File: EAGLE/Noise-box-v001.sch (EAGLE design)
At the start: 2 parts, among them J1 AVR_SPI_PROG_3X22X3_LOCK, U1 ATMEGA328P_TQFP

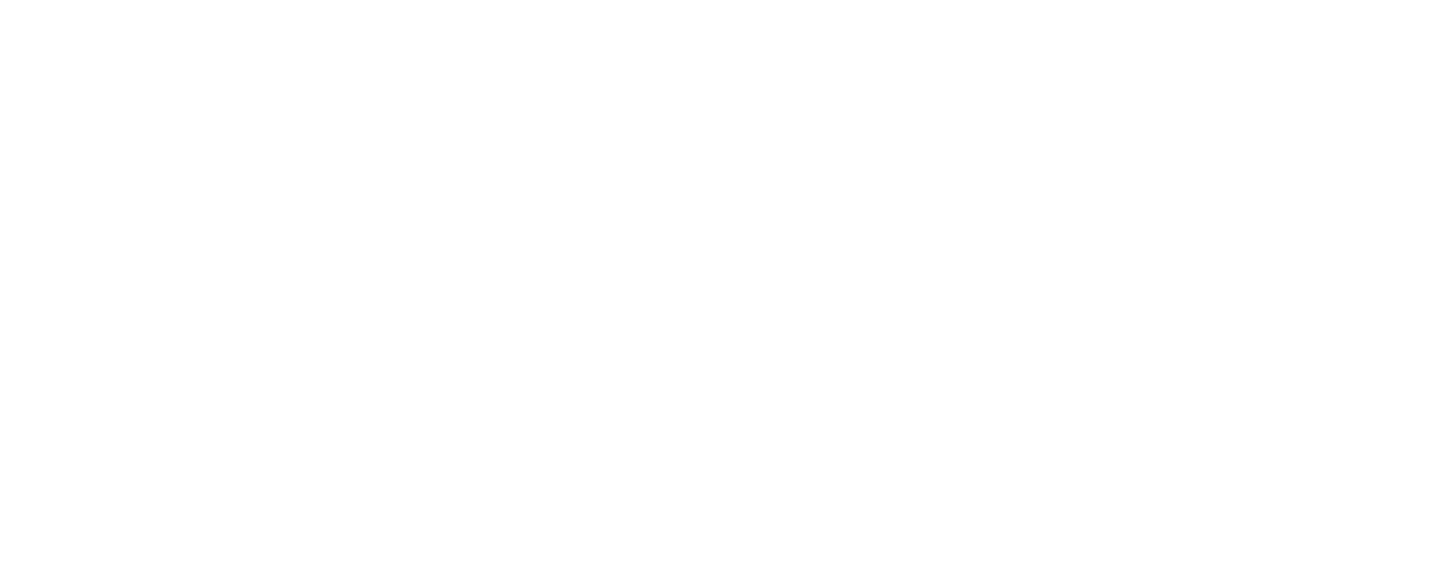
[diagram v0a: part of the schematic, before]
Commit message: Sch update - power
Added voltage regulators and supporting components.
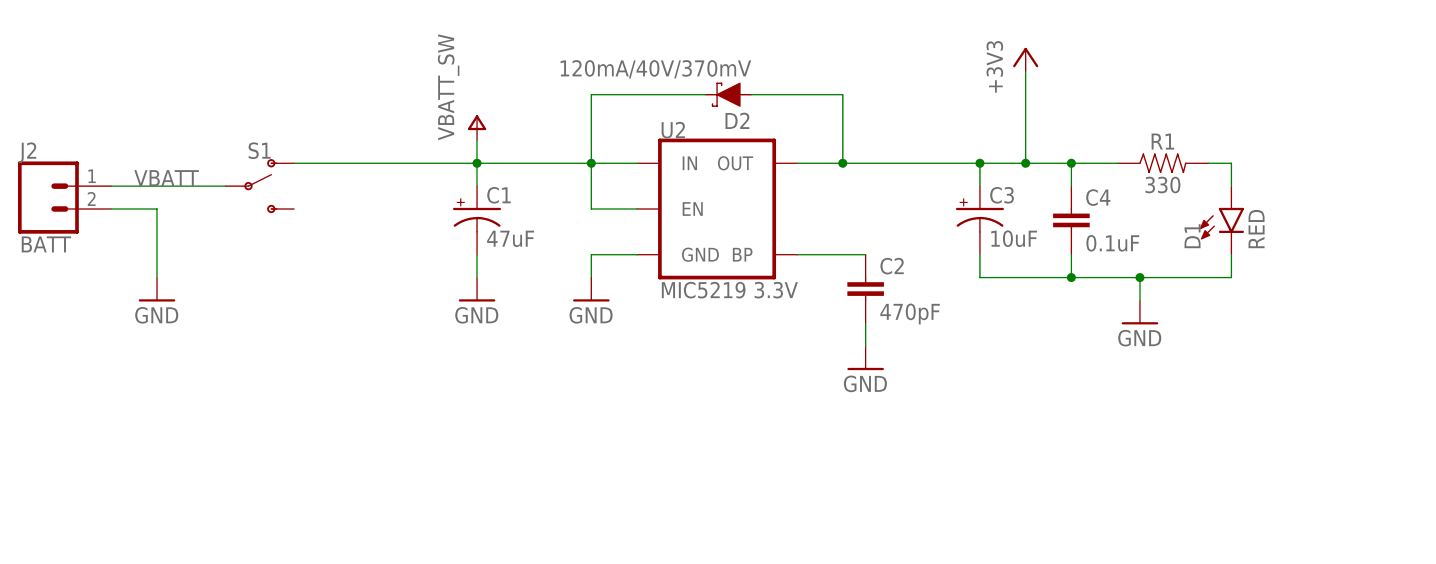
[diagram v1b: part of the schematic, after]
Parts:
- added C1: 47uF, SparkFun-Capacitors:47UF-POLAR-EIA3528-10V-10%
- added C2: 470pF, SparkFun-Capacitors:470PF-0603-50V-5%
- added C3: 10uF, SparkFun-Capacitors:10UF-POLAR-EIA3216-16V-10%(TANT)
- added C4: 0.1uF, SparkFun-Capacitors:0.1UF-0603-25V-5%
- added D1: RED, SparkFun-LED:LED-RED0603
- added D2: 120mA/40V/370mV, SparkFun-DiscreteSemi:DIODE-SCHOTTKY-RB751S40
- added J2: BATT, SparkFun-Connectors:CONN_02-JST-2MM-SMT
- added R1: 330, SparkFun-Resistors:330OHM-0603-1/10W-1%
- added S1: (no value), SparkFun-Switches:SWITCH-SPDT-SMD-RIGHT-ANGLE
- added U2: MIC5219 3.3V, SparkFun-IC-Power:V_REG_MIC52193.3V
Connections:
- new net N$2: C2.1, U2.BP
- new net N$3: D1.A, R1.2
- new net V+: C1.+, D2.C, S1.O, U2.EN, U2.IN
- new net VBATT: J2.2, S1.P
- net +3V3: now also C3.+, C4.1, D2.A, R1.1, U2.OUT
- net GND: now also C1.-, C2.2, C3.-, C4.2, D1.C, J2.1, U2.GND
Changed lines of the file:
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@@
 <part name="GND1" library="supply1" deviceset="GND" device=""/>
 <part name="J1" library="SparkFun-Connectors" deviceset="AVR_SPI_PROG_3X2" device="2X3_LOCK"/>
+<part name="J2" library="SparkFun-Connectors" deviceset="CONN_02" device="-JST-2MM-SMT" value="BATT"/>
+<part name="S1" library="SparkFun-Switches" deviceset="SWITCH-SPDT" device="-SMD-RIGHT-ANGLE"/>
+<part name="GND2" library="supply1" deviceset="GND" device=""/>
+<part name="GND3" library="supply1" deviceset="GND" device=""/>
+<part name="P+1" library="supply1" deviceset="V+" device="" value="VBATT_SW"/>
+<part name="C1" library="SparkFun-Capacitors" deviceset="47UF-POLAR" device="-EIA3528-10V-10%" value="47uF"/>
+<part name="U2" library="SparkFun-IC-Power" deviceset="V_REG_MIC5219" device="3.3V" value="MIC5219 3.3V"/>
+<part name="GND4" library="supply1" deviceset="GND" device=""/>
+<part name="C2" library="SparkFun-Capacitors" deviceset="470PF" device="-0603-50V-5%" value="470pF"/>
+<part name="GND5" library="supply1" deviceset="GND" device=""/>
+<part name="C3" library="SparkFun-Capacitors" deviceset="10UF-POLAR" device="-EIA3216-16V-10%(TANT)" value="10uF"/>
+<part name="C4" library="SparkFun-Capacitors" deviceset="0.1UF" device="-0603-25V-5%" value="0.1uF"/>
+<part name="R1" library="SparkFun-Resistors" deviceset="330OHM" device="-0603-1/10W-1%" value="330"/>
+<part name="D1" library="SparkFun-LED" deviceset="LED-RED" device="0603" value="RED"/>
+<part name="GND6" library="supply1" deviceset="GND" device=""/>
+<part name="D2" library="SparkFun-DiscreteSemi" deviceset="DIODE-SCHOTTKY" device="-RB751S40" value="120mA/40V/370mV"/>
+<part name="+3V2" library="supply1" deviceset="+3V3" device=""/>
 </parts>
 <sheets>
@@
 <instance part="GND1" gate="1" x="198.12" y="132.08"/>
 <instance part="J1" gate="G$1" x="66.04" y="170.18"/>
+<instance part="J2" gate="G$1" x="22.86" y="251.46"/>
+<instance part="S1" gate="1" x="45.72" y="254"/>
+<instance part="GND2" gate="1" x="35.56" y="241.3"/>
+<instance part="GND3" gate="1" x="71.12" y="241.3"/>
+<instance part="P+1" gate="1" x="71.12" y="261.62"/>
+<instance part="C1" gate="G$1" x="71.12" y="251.46"/>
+<instance part="U2" gate="G$1" x="99.06" y="251.46"/>
+<instance part="GND4" gate="1" x="83.82" y="241.3"/>
+<instance part="C2" gate="G$1" x="114.3" y="241.3"/>
+<instance part="GND5" gate="1" x="114.3" y="233.68"/>
+<instance part="C3" gate="G$1" x="127" y="251.46"/>
+<instance part="C4" gate="G$1" x="137.16" y="248.92"/>
+<instance part="R1" gate="G$1" x="147.32" y="256.54"/>
+<instance part="D1" gate="G$1" x="154.94" y="251.46"/>
+<instance part="GND6" gate="1" x="144.78" y="238.76"/>
+<instance part="D2" gate="G$1" x="99.06" y="264.16" rot="R180"/>
+<instance part="+3V2" gate="G$1" x="132.08" y="269.24"/>
 </instances>
 <busses>
@@
 <label x="88.9" y="172.72" size="1.778" layer="95" rot="MR0"/>
 </segment>
+<segment>
+<pinref part="U2" gate="G$1" pin="OUT"/>
+<pinref part="R1" gate="G$1" pin="1"/>
+<wire x1="106.68" y1="256.54" x2="111.76" y2="256.54" width="0.1524" layer="91"/>
+<pinref part="C3" gate="G$1" pin="+"/>
+<wire x1="111.76" y1="256.54" x2="127" y2="256.54" width="0.1524" layer="91"/>
+<wire x1="127" y1="256.54" x2="132.08" y2="256.54" width="0.1524" layer="91"/>
+<wire x1="132.08" y1="256.54" x2="137.16" y2="256.54" width="0.1524" layer="91"/>
+<wire x1="137.16" y1="256.54" x2="142.24" y2="256.54" width="0.1524" layer="91"/>
+<wire x1="127" y1="254" x2="127" y2="256.54" width="0.1524" layer="91"/>
+<junction x="127" y="256.54"/>
+<pinref part="C4" gate="G$1" pin="1"/>
+<wire x1="137.16" y1="254" x2="137.16" y2="256.54" width="0.1524" layer="91"/>
+<junction x="137.16" y="256.54"/>
+<pinref part="D2" gate="G$1" pin="A"/>
+<wire x1="111.76" y1="256.54" x2="111.76" y2="264.16" width="0.1524" layer="91"/>
+<wire x1="111.76" y1="264.16" x2="101.6" y2="264.16" width="0.1524" layer="91"/>
+<junction x="111.76" y="256.54"/>
+<pinref part="+3V2" gate="G$1" pin="+3V3"/>
+<wire x1="132.08" y1="256.54" x2="132.08" y2="266.7" width="0.1524" layer="91"/>
+<junction x="132.08" y="256.54"/>
+</segment>
 </net>
 <net name="GND" class="0">
@@
 <label x="88.9" y="167.64" size="1.778" layer="95" rot="MR0"/>
 </segment>
+<segment>
+<pinref part="J2" gate="G$1" pin="1"/>
+<pinref part="GND2" gate="1" pin="GND"/>
+<wire x1="30.48" y1="251.46" x2="35.56" y2="251.46" width="0.1524" layer="91"/>
+<wire x1="35.56" y1="251.46" x2="35.56" y2="243.84" width="0.1524" layer="91"/>
+</segment>
+<segment>
+<pinref part="GND3" gate="1" pin="GND"/>
+<pinref part="C1" gate="G$1" pin="-"/>
+<wire x1="71.12" y1="243.84" x2="71.12" y2="246.38" width="0.1524" layer="91"/>
+</segment>
+<segment>
+<pinref part="U2" gate="G$1" pin="GND"/>
+<wire x1="88.9" y1="246.38" x2="83.82" y2="246.38" width="0.1524" layer="91"/>
+<wire x1="83.82" y1="246.38" x2="83.82" y2="243.84" width="0.1524" layer="91"/>
+<pinref part="GND4" gate="1" pin="GND"/>
+</segment>
+<segment>
+<pinref part="C2" gate="G$1" pin="2"/>
+<wire x1="114.3" y1="238.76" x2="114.3" y2="236.22" width="0.1524" layer="91"/>
+<pinref part="GND5" gate="1" pin="GND"/>
+</segment>
+<segment>
+<pinref part="C4" gate="G$1" pin="2"/>
+<wire x1="137.16" y1="246.38" x2="137.16" y2="243.84" width="0.1524" layer="91"/>
+<pinref part="C3" gate="G$1" pin="-"/>
+<wire x1="127" y1="246.38" x2="127" y2="243.84" width="0.1524" layer="91"/>
+<wire x1="127" y1="243.84" x2="137.16" y2="243.84" width="0.1524" layer="91"/>
+<pinref part="D1" gate="G$1" pin="C"/>
+<wire x1="154.94" y1="246.38" x2="154.94" y2="243.84" width="0.1524" layer="91"/>
+<wire x1="137.16" y1="243.84" x2="144.78" y2="243.84" width="0.1524" layer="91"/>
+<junction x="137.16" y="243.84"/>
+<pinref part="GND6" gate="1" pin="GND"/>
+<wire x1="144.78" y1="243.84" x2="154.94" y2="243.84" width="0.1524" layer="91"/>
+<wire x1="144.78" y1="241.3" x2="144.78" y2="243.84" width="0.1524" layer="91"/>
+<junction x="144.78" y="243.84"/>
+</segment>
 </net>
 <net name="MOSI" class="0">
@@
 </segment>
 </net>
+<net name="VBATT" class="0">
+<segment>
+<pinref part="J2" gate="G$1" pin="2"/>
+<pinref part="S1" gate="1" pin="P"/>
+<wire x1="30.48" y1="254" x2="43.18" y2="254" width="0.1524" layer="91"/>
+<label x="33.02" y="254" size="1.778" layer="95"/>
+</segment>
+</net>
+<net name="V+" class="0">
+<segment>
+<pinref part="P+1" gate="1" pin="V+"/>
+<pinref part="C1" gate="G$1" pin="+"/>
+<wire x1="71.12" y1="259.08" x2="71.12" y2="256.54" width="0.1524" layer="91"/>
+<pinref part="S1" gate="1" pin="O"/>
+<wire x1="71.12" y1="256.54" x2="71.12" y2="254" width="0.1524" layer="91"/>
+<wire x1="50.8" y1="256.54" x2="71.12" y2="256.54" width="0.1524" layer="91"/>
+<junction x="71.12" y="256.54"/>
+<pinref part="U2" gate="G$1" pin="IN"/>
+<wire x1="71.12" y1="256.54" x2="83.82" y2="256.54" width="0.1524" layer="91"/>
+<pinref part="U2" gate="G$1" pin="EN"/>
+<wire x1="83.82" y1="256.54" x2="88.9" y2="256.54" width="0.1524" layer="91"/>
+<wire x1="88.9" y1="251.46" x2="83.82" y2="251.46" width="0.1524" layer="91"/>
+<wire x1="83.82" y1="251.46" x2="83.82" y2="256.54" width="0.1524" layer="91"/>
+<junction x="83.82" y="256.54"/>
+<pinref part="D2" gate="G$1" pin="C"/>
+<wire x1="96.52" y1="264.16" x2="83.82" y2="264.16" width="0.1524" layer="91"/>
+<wire x1="83.82" y1="264.16" x2="83.82" y2="256.54" width="0.1524" layer="91"/>
+</segment>
+</net>
+<net name="N$2" class="0">
+<segment>
+<pinref part="U2" gate="G$1" pin="BP"/>
+<pinref part="C2" gate="G$1" pin="1"/>
+<wire x1="106.68" y1="246.38" x2="114.3" y2="246.38" width="0.1524" layer="91"/>
+</segment>
+</net>
+<net name="N$3" class="0">
+<segment>
+<pinref part="R1" gate="G$1" pin="2"/>
+<pinref part="D1" gate="G$1" pin="A"/>
+<wire x1="152.4" y1="256.54" x2="154.94" y2="256.54" width="0.1524" layer="91"/>
+<wire x1="154.94" y1="256.54" x2="154.94" y2="254" width="0.1524" layer="91"/>
+</segment>
+</net>

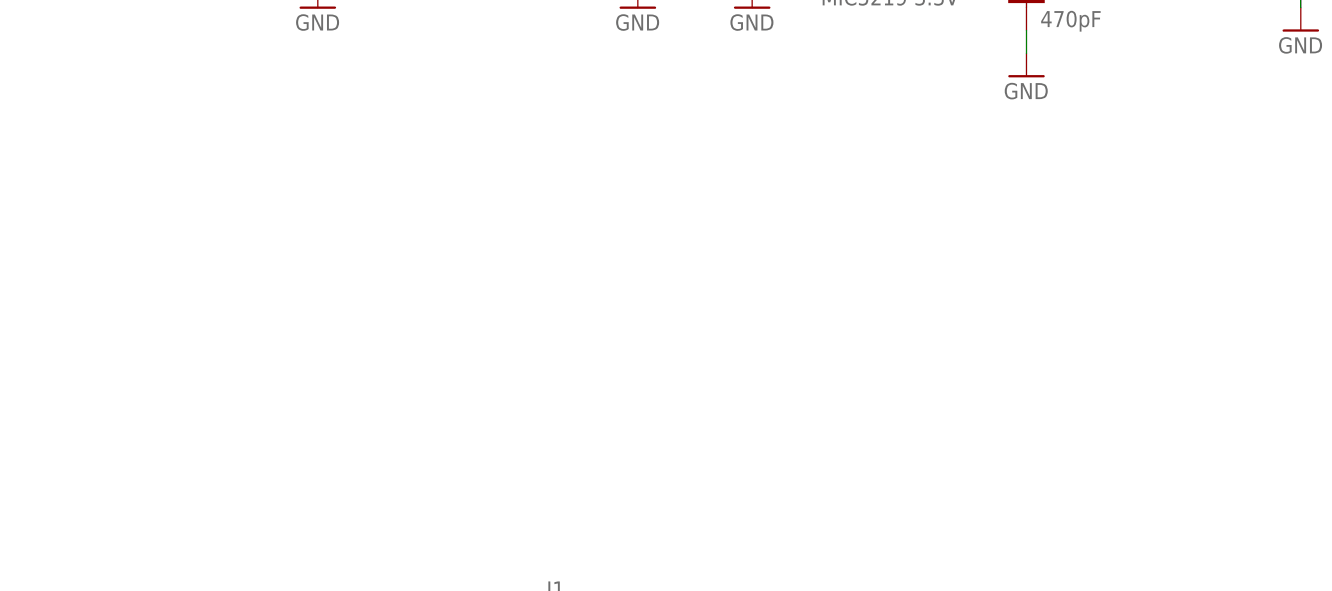
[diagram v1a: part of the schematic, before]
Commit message: Schematic work
Added regulator, battery charging circuit
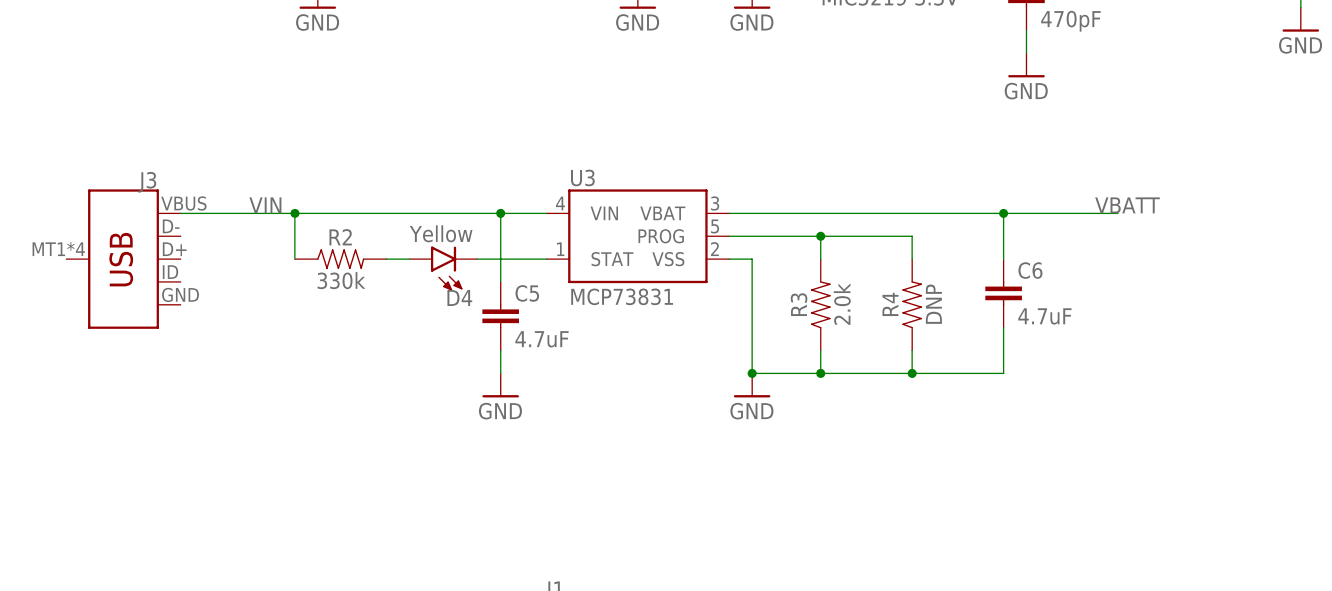
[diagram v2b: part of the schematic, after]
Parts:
- added C5, C6: 4.7uF, SparkFun-Capacitors:4.7UF0603
- added D4: Yellow, SparkFun-LED:LED-YELLOW0603
- added J3: (no value), SparkFun-Connectors:USB_MICRO-B_SMT
- added R2: 330k, SparkFun-Resistors:330KOHM-0603-1/10W-1%
- added R3: 2.0k, SparkFun-Resistors:2.0KOHM-0603-1/10W-5%
- added R4: DNP, SparkFun-Resistors:2.0KOHM-0603-1/10W-5%
- added U3: MCP73831, SparkFun-IC-Power:MCP73831
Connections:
- new net N$1: D4.A, R2.2
- new net N$4: R3.2, R4.2, U3.PROG
- new net N$5: D4.C, U3.STAT
- new net VIN: C5.1, J3.VBUS, R2.1, U3.VIN
- net GND: now also C5.2, C6.2, R3.1, R4.1, U3.VSS
- net VBATT: now also C6.1, U3.VBAT
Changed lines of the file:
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@@
 <part name="D2" library="SparkFun-DiscreteSemi" deviceset="DIODE-SCHOTTKY" device="-RB751S40" value="120mA/40V/370mV"/>
 <part name="+3V2" library="supply1" deviceset="+3V3" device=""/>
+<part name="J3" library="SparkFun-Connectors" deviceset="USB_MICRO-B" device="_SMT"/>
+<part name="U3" library="SparkFun-IC-Power" deviceset="MCP73831" device=""/>
+<part name="D4" library="SparkFun-LED" deviceset="LED-YELLOW" device="0603" value="Yellow"/>
+<part name="R2" library="SparkFun-Resistors" deviceset="330KOHM" device="-0603-1/10W-1%" value="330k"/>
+<part name="C5" library="SparkFun-Capacitors" deviceset="4.7UF" device="0603" value="4.7uF"/>
+<part name="R3" library="SparkFun-Resistors" deviceset="2.0KOHM" device="-0603-1/10W-5%" value="2.0k"/>
+<part name="R4" library="SparkFun-Resistors" deviceset="2.0KOHM" device="-0603-1/10W-5%" value="DNP"/>
+<part name="C6" library="SparkFun-Capacitors" deviceset="4.7UF" device="0603" value="4.7uF"/>
+<part name="GND7" library="supply1" deviceset="GND" device=""/>
+<part name="GND8" library="supply1" deviceset="GND" device=""/>
 </parts>
 <sheets>
@@
 <instance part="D2" gate="G$1" x="99.06" y="264.16" rot="R180"/>
 <instance part="+3V2" gate="G$1" x="132.08" y="269.24"/>
+<instance part="J3" gate="G$1" x="15.24" y="213.36" rot="MR0"/>
+<instance part="U3" gate="G$1" x="71.12" y="215.9"/>
+<instance part="D4" gate="G$1" x="48.26" y="213.36" rot="R90"/>
+<instance part="R2" gate="G$1" x="38.1" y="213.36"/>
+<instance part="C5" gate="G$1" x="55.88" y="205.74"/>
+<instance part="R3" gate="G$1" x="91.44" y="208.28" rot="R90"/>
+<instance part="R4" gate="G$1" x="101.6" y="208.28" rot="R90"/>
+<instance part="C6" gate="G$1" x="111.76" y="208.28"/>
+<instance part="GND7" gate="1" x="55.88" y="198.12"/>
+<instance part="GND8" gate="1" x="83.82" y="198.12"/>
 </instances>
 <busses>
@@
 <junction x="144.78" y="243.84"/>
 </segment>
+<segment>
+<pinref part="C5" gate="G$1" pin="2"/>
+<pinref part="GND7" gate="1" pin="GND"/>
+<wire x1="55.88" y1="203.2" x2="55.88" y2="200.66" width="0.1524" layer="91"/>
+</segment>
+<segment>
+<pinref part="U3" gate="G$1" pin="VSS"/>
+<pinref part="GND8" gate="1" pin="GND"/>
+<wire x1="81.28" y1="213.36" x2="83.82" y2="213.36" width="0.1524" layer="91"/>
+<wire x1="83.82" y1="213.36" x2="83.82" y2="200.66" width="0.1524" layer="91"/>
+<pinref part="R3" gate="G$1" pin="1"/>
+<wire x1="91.44" y1="203.2" x2="91.44" y2="200.66" width="0.1524" layer="91"/>
+<wire x1="91.44" y1="200.66" x2="83.82" y2="200.66" width="0.1524" layer="91"/>
+<junction x="83.82" y="200.66"/>
+<pinref part="R4" gate="G$1" pin="1"/>
+<wire x1="101.6" y1="203.2" x2="101.6" y2="200.66" width="0.1524" layer="91"/>
+<wire x1="101.6" y1="200.66" x2="91.44" y2="200.66" width="0.1524" layer="91"/>
+<junction x="91.44" y="200.66"/>
+<pinref part="C6" gate="G$1" pin="2"/>
+<wire x1="111.76" y1="205.74" x2="111.76" y2="200.66" width="0.1524" layer="91"/>
+<wire x1="111.76" y1="200.66" x2="101.6" y2="200.66" width="0.1524" layer="91"/>
+<junction x="101.6" y="200.66"/>
+</segment>
 </net>
 <net name="MOSI" class="0">
@@
 <wire x1="30.48" y1="254" x2="43.18" y2="254" width="0.1524" layer="91"/>
 <label x="33.02" y="254" size="1.778" layer="95"/>
+</segment>
+<segment>
+<pinref part="U3" gate="G$1" pin="VBAT"/>
+<wire x1="81.28" y1="218.44" x2="111.76" y2="218.44" width="0.1524" layer="91"/>
+<pinref part="C6" gate="G$1" pin="1"/>
+<wire x1="111.76" y1="218.44" x2="124.46" y2="218.44" width="0.1524" layer="91"/>
+<wire x1="111.76" y1="213.36" x2="111.76" y2="218.44" width="0.1524" layer="91"/>
+<junction x="111.76" y="218.44"/>
+<label x="121.92" y="218.44" size="1.778" layer="95"/>
 </segment>
 </net>
@@
 </segment>
 </net>
+<net name="N$1" class="0">
+<segment>
+<pinref part="R2" gate="G$1" pin="2"/>
+<pinref part="D4" gate="G$1" pin="A"/>
+<wire x1="45.72" y1="213.36" x2="43.18" y2="213.36" width="0.1524" layer="91"/>
+</segment>
+</net>
+<net name="VIN" class="0">
+<segment>
+<pinref part="J3" gate="G$1" pin="VBUS"/>
+<pinref part="C5" gate="G$1" pin="1"/>
+<wire x1="20.32" y1="218.44" x2="33.02" y2="218.44" width="0.1524" layer="91"/>
+<wire x1="33.02" y1="218.44" x2="55.88" y2="218.44" width="0.1524" layer="91"/>
+<wire x1="55.88" y1="218.44" x2="55.88" y2="210.82" width="0.1524" layer="91"/>
+<pinref part="R2" gate="G$1" pin="1"/>
+<wire x1="33.02" y1="213.36" x2="33.02" y2="218.44" width="0.1524" layer="91"/>
+<junction x="33.02" y="218.44"/>
+<pinref part="U3" gate="G$1" pin="VIN"/>
+<wire x1="55.88" y1="218.44" x2="60.96" y2="218.44" width="0.1524" layer="91"/>
+<junction x="55.88" y="218.44"/>
+<label x="27.94" y="218.44" size="1.778" layer="95"/>
+</segment>
+</net>
+<net name="N$5" class="0">
+<segment>
+<pinref part="D4" gate="G$1" pin="C"/>
+<pinref part="U3" gate="G$1" pin="STAT"/>
+<wire x1="53.34" y1="213.36" x2="60.96" y2="213.36" width="0.1524" layer="91"/>
+</segment>
+</net>
+<net name="N$4" class="0">
+<segment>
+<pinref part="U3" gate="G$1" pin="PROG"/>
+<pinref part="R3" gate="G$1" pin="2"/>
+<wire x1="81.28" y1="215.9" x2="91.44" y2="215.9" width="0.1524" layer="91"/>
+<wire x1="91.44" y1="215.9" x2="91.44" y2="213.36" width="0.1524" layer="91"/>
+<pinref part="R4" gate="G$1" pin="2"/>
+<wire x1="91.44" y1="215.9" x2="101.6" y2="215.9" width="0.1524" layer="91"/>
+<wire x1="101.6" y1="215.9" x2="101.6" y2="213.36" width="0.1524" layer="91"/>
+<junction x="91.44" y="215.9"/>
+</segment>
+</net>
